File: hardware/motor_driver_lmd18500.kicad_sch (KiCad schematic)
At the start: 11 parts, among them J4 Screw_Terminal_01x02, J5 Screw_Terminal_01x02, M1 Motor_DC, U2 LMD18200T_NOPB

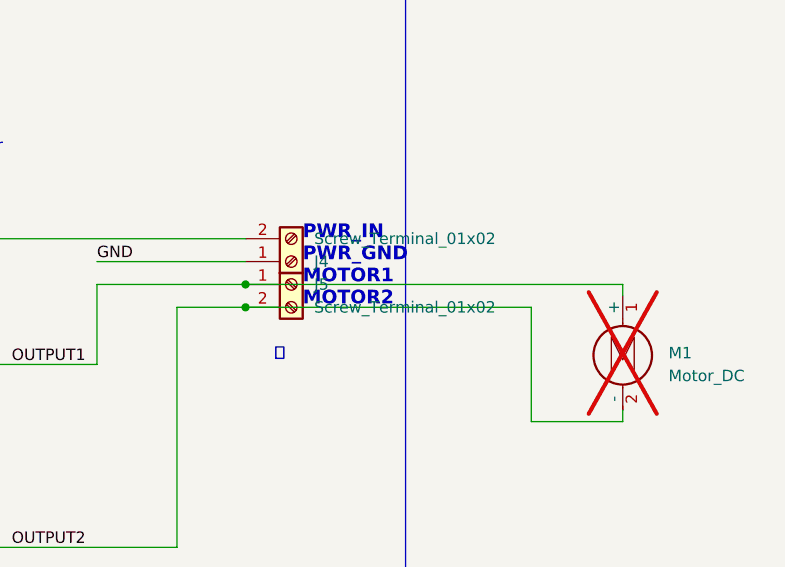
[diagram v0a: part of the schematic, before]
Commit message: feat: update to kicad 10 and migrate old references to kml
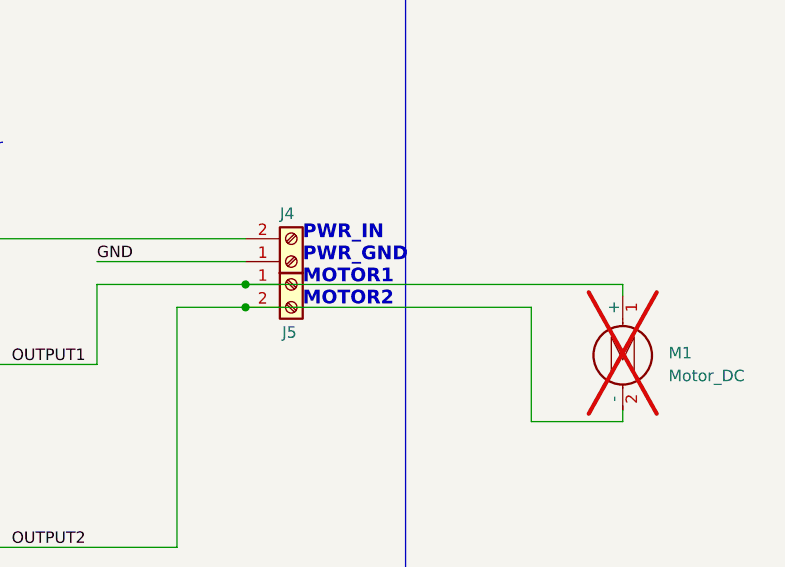
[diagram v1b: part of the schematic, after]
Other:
- note removed: "🔁"
